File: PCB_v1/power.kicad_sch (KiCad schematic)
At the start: 22 parts, among them J3 S2B-PH-K-SLFSN, J4 Conn_01x05_Pin, J5 Conn_01x05_Pin, U2 BQ25185DLHR, U3 BQ27441-G1

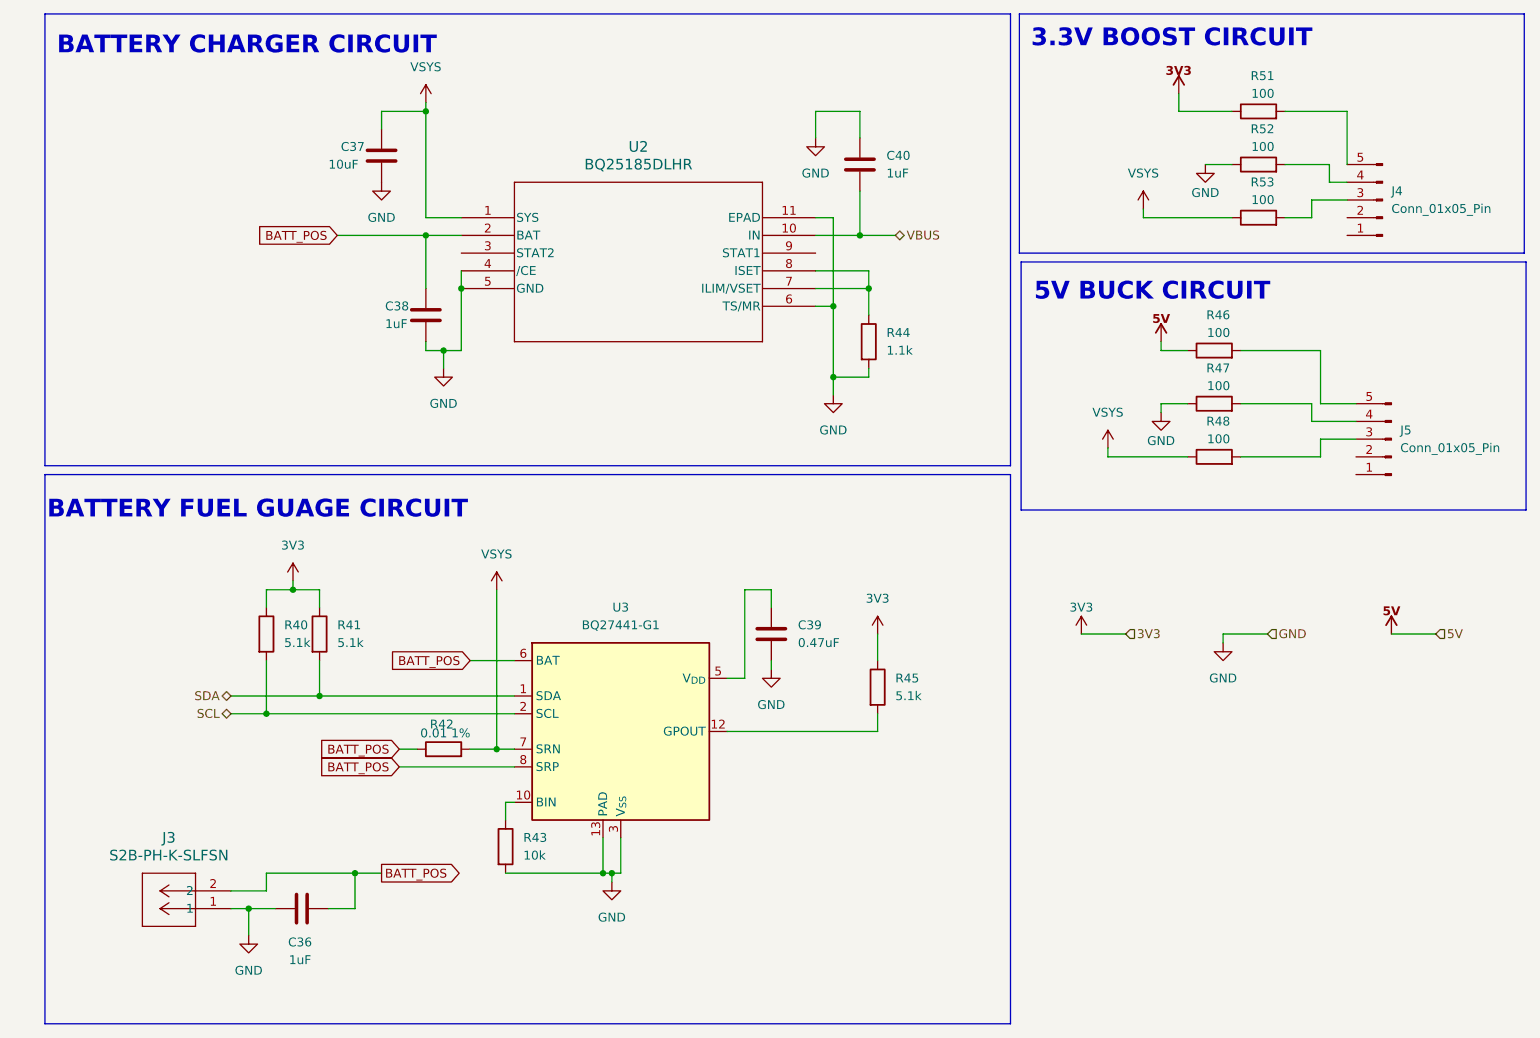
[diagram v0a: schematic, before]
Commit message: adding the parts library
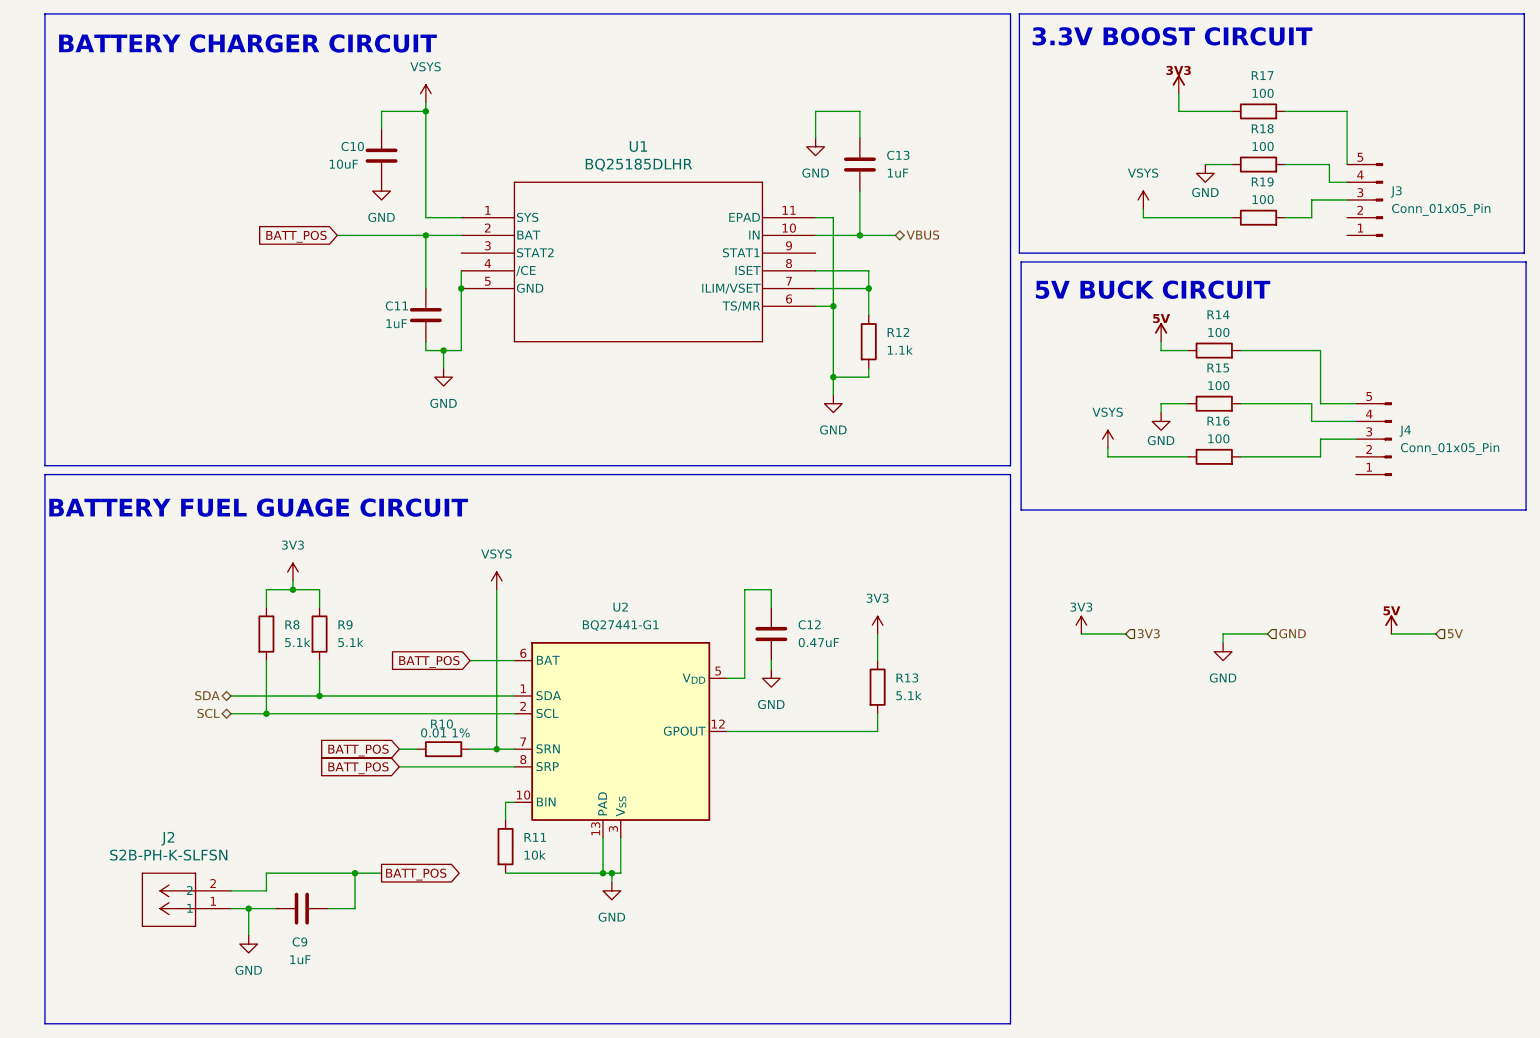
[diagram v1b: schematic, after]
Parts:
- C10: renamed from C37; footprint (none) -> Capacitor_SMD:C_0805_2012Metric
- C11: renamed from C38; footprint (none) -> Capacitor_SMD:C_0805_2012Metric
- C12: renamed from C39; footprint (none) -> Capacitor_SMD:C_0805_2012Metric
- C13: renamed from C40; footprint (none) -> Capacitor_SMD:C_0805_2012Metric
- C9: renamed from C36; footprint (none) -> Capacitor_SMD:C_0805_2012Metric
- R10: renamed from R42; footprint (none) -> Resistor_SMD:R_0805_2012Metric
- R11: renamed from R43; footprint (none) -> Resistor_SMD:R_0805_2012Metric
- R12: renamed from R44; footprint (none) -> Resistor_SMD:R_0805_2012Metric
- R13: renamed from R45; footprint (none) -> Resistor_SMD:R_0805_2012Metric
- R14: renamed from R46; footprint (none) -> Resistor_SMD:R_0805_2012Metric
- R15: renamed from R47; footprint (none) -> Resistor_SMD:R_0805_2012Metric
- R16: renamed from R48; footprint (none) -> Resistor_SMD:R_0805_2012Metric
- R17: renamed from R51; footprint (none) -> Resistor_SMD:R_0805_2012Metric
- R18: renamed from R52; footprint (none) -> Resistor_SMD:R_0805_2012Metric
- R19: renamed from R53; footprint (none) -> Resistor_SMD:R_0805_2012Metric
- R8: renamed from R40; footprint (none) -> Resistor_SMD:R_0805_2012Metric
- R9: renamed from R41; footprint (none) -> Resistor_SMD:R_0805_2012Metric
- U2: renamed from U3; footprint Package_SON:Texas_S-PDSO-N12 -> Texas_S-PDSO-N12
- renumbered J3 to J2, J4 to J3, J5 to J4, U2 to U1

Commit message: Updated power schematic :D
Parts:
- added R60: 0, Resistor_SMD:R_0805_2012Metric, symbol Device:R
- J3: footprint Connector_PinHeader_1.00mm:PinHeader_1x05_P1.00mm_Vertical -> Connector_PinHeader_2.54mm:PinHeader_1x05_P2.54mm_Vertical
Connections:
- net BATT_POS: now also R60.2; no longer C9.2, J2.2
- new net: C9.2, J2.2, R60.1
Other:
- note added: "3.3V BUCK CIRCUIT"
- note added: "5V BOOST CIRCUIT"
- note added: "this is where the power switch goes"
- note removed: "3.3V BOOST CIRCUIT"
- note removed: "5V BUCK CIRCUIT"
- moved on the sheet: C9, J2
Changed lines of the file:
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@@
 	)
 	(junction
-		(at 57.15 135.89)
-		(diameter 0)
-		(color 0 0 0 0)
-	)
-	(junction
 		(at 125.73 64.77)
 		(diameter 0)
@@
 	)
 	(junction
-		(at 41.91 140.97)
+		(at 36.83 140.97)
 		(diameter 0)
 		(color 0 0 0 0)
@@
 	)
 	(junction
+		(at 49.53 135.89)
+		(diameter 0)
+		(color 0 0 0 0)
+	)
+	(junction
 		(at 44.45 113.03)
 		(diameter 0)
@@
 	(wire
 		(pts
-			(xy 41.91 140.97) (xy 45.72 140.97)
+			(xy 36.83 140.97) (xy 40.64 140.97)
+		)
+		(stroke
+			(width 0)
+			(type default)
+		)
+	)
+	(wire
+		(pts
+			(xy 59.69 135.89) (xy 62.23 135.89)
 		)
 		(stroke
@@
 	(wire
 		(pts
-			(xy 57.15 135.89) (xy 60.96 135.89)
-		)
-		(stroke
-			(width 0)
-			(type default)
-		)
-	)
-	(wire
-		(pts
 			(xy 39.37 110.49) (xy 52.07 110.49)
 		)
@@
 	(wire
 		(pts
-			(xy 44.45 135.89) (xy 57.15 135.89)
+			(xy 39.37 135.89) (xy 49.53 135.89)
 		)
 		(stroke
@@
 	(wire
 		(pts
-			(xy 41.91 140.97) (xy 41.91 144.78)
+			(xy 36.83 140.97) (xy 36.83 144.78)
 		)
 		(stroke
@@
 	(wire
 		(pts
+			(xy 49.53 135.89) (xy 52.07 135.89)
+		)
+		(stroke
+			(width 0)
+			(type default)
+		)
+	)
+	(wire
+		(pts
 			(xy 73.66 118.11) (xy 77.47 118.11)
 		)
@@
 	(wire
 		(pts
-			(xy 53.34 140.97) (xy 57.15 140.97)
+			(xy 48.26 140.97) (xy 49.53 140.97)
 		)
 		(stroke
@@
 	(wire
 		(pts
-			(xy 57.15 135.89) (xy 57.15 140.97)
+			(xy 49.53 135.89) (xy 49.53 140.97)
 		)
 		(stroke
@@
 	(wire
 		(pts
-			(xy 44.45 135.89) (xy 44.45 138.43)
+			(xy 39.37 135.89) (xy 39.37 138.43)
 		)
 		(stroke
@@
 	(wire
 		(pts
-			(xy 44.45 138.43) (xy 39.37 138.43)
+			(xy 39.37 138.43) (xy 34.29 138.43)
 		)
 		(stroke
@@
 	(wire
 		(pts
-			(xy 39.37 140.97) (xy 41.91 140.97)
+			(xy 34.29 140.97) (xy 36.83 140.97)
 		)
 		(stroke
@@
 		)
 	)
-	(text "3.3V BOOST CIRCUIT"
+	(text "3.3V BUCK CIRCUIT"
 		(exclude_from_sim no)
-		(at 174.244 16.256 0)
+		(at 172.212 16.256 0)
 		(effects
 			(font
@@
 		)
 	)
-	(text "5V BUCK CIRCUIT"
+	(text "this is where the power\n switch goes\n"
+		(exclude_from_sim no)
+		(at 63.5 140.716 0)
+		(effects
+			(font
+				(size 1.27 1.27)
+			)
+		)
+	)
+	(text "5V BOOST CIRCUIT"
 		(exclude_from_sim no)
 		(at 171.45 52.578 0)
@@
 	(global_label "BATT_POS"
 		(shape output)
-		(at 60.96 135.89 0)
+		(at 62.23 135.89 0)
 		(fields_autoplaced yes)
 		(effects
@@
 		)
 		(property "Intersheetrefs" "${INTERSHEET_REFS}"
-			(at 73.0166 135.89 0)
+			(at 74.2866 135.89 0)
 			(effects
 				(font
@@
 	)
 	(symbol
+		(lib_id "Device:R")
+		(at 55.88 135.89 90)
+		(unit 1)
+		(exclude_from_sim no)
+		(in_bom yes)
+		(on_board yes)
+		(dnp no)
+		(property "Reference" "R60"
+			(at 58.166 130.81 90)
+			(effects
+				(font
+					(size 1.27 1.27)
+				)
+				(justify left)
+			)
+		)
+		(property "Value" "0"
+			(at 58.166 133.35 90)
+			(effects
+				(font
+					(size 1.27 1.27)
+				)
+				(justify left)
+			)
+		)
+		(property "Footprint" "Resistor_SMD:R_0805_2012Metric"
+			(at 55.88 137.668 90)
+			(effects
+				(font
+					(size 1.27 1.27)
+				)
+				(hide yes)
+			)
+		)
+		(property "Datasheet" "~"
+			(at 55.88 135.89 0)
+			(effects
+				(font
+					(size 1.27 1.27)
+				)
+				(hide yes)
+			)
+		)
+		(property "Description" "Resistor"
+			(at 55.88 135.89 0)
+			(effects
+				(font
+					(size 1.27 1.27)
+				)
+				(hide yes)
+			)
+		)
+		(pin "2"
+		)
+		(pin "1"
+		)
+		(instances
+			(project "tuner time"
+				(path "/353cef6a-fb6e-40d9-89f8-eb54b7aa5118/c1a9b430-6647-4f38-9d0b-e66a572eaaf0"
+					(reference "R60")
+					(unit 1)
+				)
+			)
+		)
+	)
+	(symbol
 		(lib_id "power:+3.3V")
 		(at 67.31 25.4 0)
@@
 	(symbol
 		(lib_id "power:GND")
-		(at 41.91 144.78 0)
+		(at 36.83 144.78 0)
 		(unit 1)
 		(exclude_from_sim no)
@@
 		(fields_autoplaced yes)
 		(property "Reference" "#PWR036"
-			(at 41.91 151.13 0)
+			(at 36.83 151.13 0)
 			(effects
 				(font
@@
 		)
 		(property "Value" "GND"
-			(at 41.91 149.86 0)
+			(at 36.83 149.86 0)
 			(effects
 				(font
@@
 		)
 		(property "Footprint" ""
-			(at 41.91 144.78 0)
+			(at 36.83 144.78 0)
 			(effects
 				(font
@@
 		)
 		(property "Datasheet" ""
-			(at 41.91 144.78 0)
+			(at 36.83 144.78 0)
 			(effects
 				(font
@@
 		)
 		(property "Description" "Power symbol creates a global label with name \"GND\" , ground"
-			(at 41.91 144.78 0)
+			(at 36.83 144.78 0)
 			(effects
 				(font
@@
 	(symbol
 		(lib_id "Device:C")
-		(at 49.53 140.97 90)
+		(at 44.45 140.97 90)
 		(unit 1)
 		(exclude_from_sim no)
@@
 		(dnp no)
 		(property "Reference" "C9"
-			(at 49.276 145.796 90)
+			(at 44.196 145.796 90)
 			(effects
 				(font
@@
 		)
 		(property "Value" "1uF"
-			(at 49.276 148.336 90)
+			(at 44.196 148.336 90)
 			(effects
 				(font
@@
 		)
 		(property "Footprint" "Capacitor_SMD:C_0805_2012Metric"
-			(at 53.34 140.0048 0)
+			(at 48.26 140.0048 0)
 			(effects
 				(font
@@
 		)
 		(property "Datasheet" "~"
-			(at 49.53 140.97 0)
+			(at 44.45 140.97 0)
 			(effects
 				(font
@@
 		)
 		(property "Description" "Unpolarized capacitor"
-			(at 49.53 140.97 0)
+			(at 44.45 140.97 0)
 			(effects
 				(font
@@
 	(symbol
 		(lib_id "2025-02-12_12-07-11:S2B-PH-K-SLFSN")
-		(at 39.37 140.97 180)
+		(at 34.29 140.97 180)
 		(unit 1)
 		(exclude_from_sim no)
@@
 		(fields_autoplaced yes)
 		(property "Reference" "J2"
-			(at 30.48 130.81 0)
+			(at 25.4 130.81 0)
 			(effects
 				(font
@@
 		)
 		(property "Value" "S2B-PH-K-SLFSN"
-			(at 30.48 133.35 0)
+			(at 25.4 133.35 0)
 			(effects
 				(font
@@
 		)
 		(property "Footprint" "CONN_S2B-PH-K-S_JST"
-			(at 39.37 140.97 0)
+			(at 34.29 140.97 0)
 			(effects
 				(font
@@
 		)
 		(property "Datasheet" "S2B-PH-K-SLFSN"
-			(at 39.37 140.97 0)
+			(at 34.29 140.97 0)
 			(effects
 				(font
@@
 		)
 		(property "Description" ""
-			(at 39.37 140.97 0)
+			(at 34.29 140.97 0)
 			(effects
 				(font
@@
 			)
 		)
-		(property "Footprint" "Connector_PinHeader_1.00mm:PinHeader_1x05_P1.00mm_Vertical"
+		(property "Footprint" "Connector_PinHeader_2.54mm:PinHeader_1x05_P2.54mm_Vertical"
 			(at 204.47 39.37 0)
 			(effects

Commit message: PCB updates
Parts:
- removed R60: 0, Resistor_SMD:R_0805_2012Metric, symbol Device:R
- added SW1: SW_SPST, Parts_Library:JST_B2B-XH-A, symbol Switch:SW_SPST
- J6: renamed from J4; footprint Connector_PinHeader_1.00mm:PinHeader_1x05_P1.00mm_Vertical -> Connector_PinHeader_2.54mm:PinHeader_1x05_P2.54mm_Vertical
- R4: renamed from R10; MFP (none) -> WSL0805R0100FEA1
- U3: renamed from U2; footprint Texas_S-PDSO-N12 -> Package_SON:Texas_S-PDSO-N12
- renumbered C9 to C1, C10 to C2, C11 to C3, C12 to C4, C13 to C5, J2 to J4, J3 to J5, R16 to R10, R17 to R11, R18 to R12, R19 to R13, R8 to R2, R9 to R3, R11 to R5, R12 to R6, R13 to R7, R14 to R8, R15 to R9, U1 to U2
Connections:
- net BATT_POS: now also SW1.2 (B)
- net GND: no longer R9.1
- net at C1.2, J4.2: now also SW1.1 (A)
- new net AGND: R9.1
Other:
- note added: "The Footprint for the power switch is a 2 pin- 2.54 mm jst connector"
- note removed: "this is where the power switch goes"

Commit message: adjusted placments
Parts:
- removed J4: S2B-PH-K-SLFSN, CONN_S2B-PH-K-S_JST, symbol 2025-02-12_12-07-11:S2B-PH-K-SLFSN
- removed R10, R11, R12, R13, R8, R9: 100, Resistor_SMD:R_0805_2012Metric, symbol Device:R
- added J3: S2B-PH-K-SLFSN, CONN_S2B-PH-K-S_JST, symbol 2025-02-12_12-07-11:S2B-PH-K-SLFSN
- renumbered J5 to J4, J6 to J5, R2 to R4, R3 to R5, R4 to R6, R5 to R7, R6 to R8, R7 to R9
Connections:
- net 3V3: now also J4.5 (Pin_5)
- net 5V: now also J5.5 (Pin_5)
- net AGND: now also J5.4 (Pin_4)
- net GND: now also J4.4 (Pin_4), J3.1
- net VSYS: now also J4.3 (Pin_3), J5.3 (Pin_3)
- net at C1.2, SW1.1 (A): now also J3.2

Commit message: Power Layout done
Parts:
- added D8, D9: Red, LED_SMD:LED_0805_2012Metric_Pad1.15x1.40mm_HandSolder, symbol Device:LED
- added R21: 680, Resistor_SMD:R_0805_2012Metric, symbol Device:R
- added R22: 1k, Resistor_SMD:R_0805_2012Metric, symbol Device:R
- added R23: 10k, Resistor_SMD:R_0805_2012Metric, symbol Device:R
- C2: value 10uF -> 22uF
- C3, C5: value 1uF -> 22uF
- J3: value S2B-PH-K-SLFSN -> JST_B2B-XH-A; footprint CONN_S2B-PH-K-S_JST -> JST_B2B-XH-A
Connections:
- net BATT_POS: now also C1.2; no longer C3.1, U2.2 (BAT)
- net GND: now also R23.2; no longer U2.6 (TS/MR)
- net VSYS: now also D8.2 (A), D9.2 (A); no longer R6.2, U3.7 (SRN)
- net BAT_EMPTY: now reaches R9.2, U3.12 (GPOUT)
- net at J3.2, SW1.1 (A): no longer C1.2
- net STATS2: now reaches U2.3 (STAT2)
- net STATS2: now also R21.1
- net STATS1: now reaches U2.9 (STAT1)
- net STATS1: now also R22.1
- new net: D8.1 (K), R21.2
- new net: D9.1 (K), R22.2
- new net: R23.1, U2.6 (TS/MR)
- new net VBAT: C3.1, R6.2, U2.2 (BAT), U3.7 (SRN)
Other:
- moved on the sheet: C1, R8

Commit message: before annonation reset
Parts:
- J3: MFP (none) -> S2B-PH-K-SLFSN
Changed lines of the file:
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@@
 			)
 		)
-		(property "Datasheet" "S2B-PH-K-SLFSN"
+		(property "Datasheet" ""
 			(at 34.29 140.97 0)
 			(effects
@@
 			)
 		)
-		(property "MFP" ""
+		(property "MFP" "S2B-PH-K-SLFSN"
 			(at 34.29 140.97 0)
 			(effects

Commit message: pushing BOM
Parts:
- J4, J5: MFP (none) -> Genereic 5 pin 2.56mm
- SW1: footprint Parts_Library:JST_B2B-XH-A -> JST_B2B-PH-K-S; MFP (none) -> JST_B2B-PH-K-S
- U1: renamed from U2; MFP (none) -> BQ25185DLHR
- U2: renamed from U3; MFP (none) -> BQ27441-G1
- renumbered C2 to C1, C1 to C2, D8 to D4, D9 to D5, R23 to R10, R9 to R11, R8 to R12, R21 to R4, R22 to R5, R4 to R6, R5 to R7, R6 to R8, R7 to R9
